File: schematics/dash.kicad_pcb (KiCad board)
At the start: 2 copper layers, 43.1 x 26.8 mm, 32 parts, among them J1 BATT_CONN, J2 EXTERNAL_TRIGGER, J3 USB_OTG, J4 Conn_01x08, J5 Conn_01x08, SW1 SW_Push, U1 ESP-12E, U2 ch340g, U3 MCP73833, U4 HT7333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

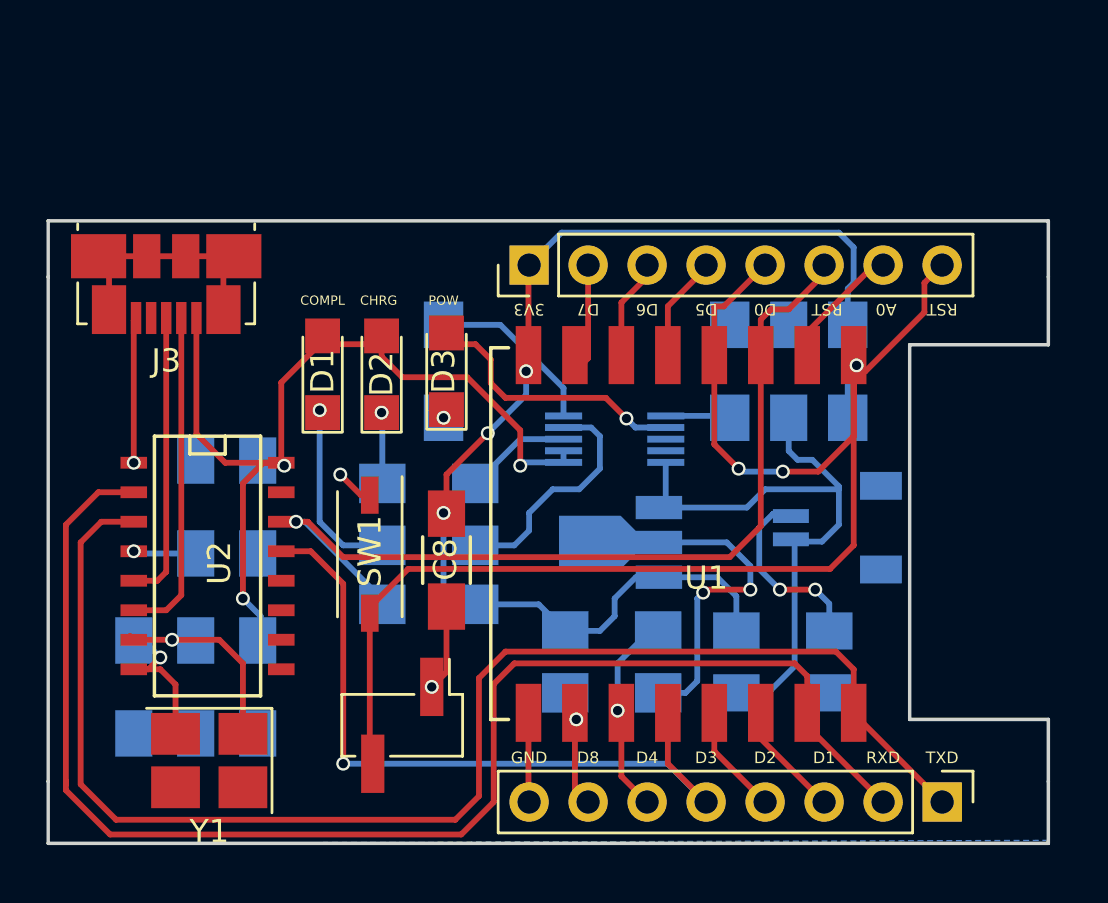
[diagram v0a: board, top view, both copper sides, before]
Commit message: [enh] Changed pcb size
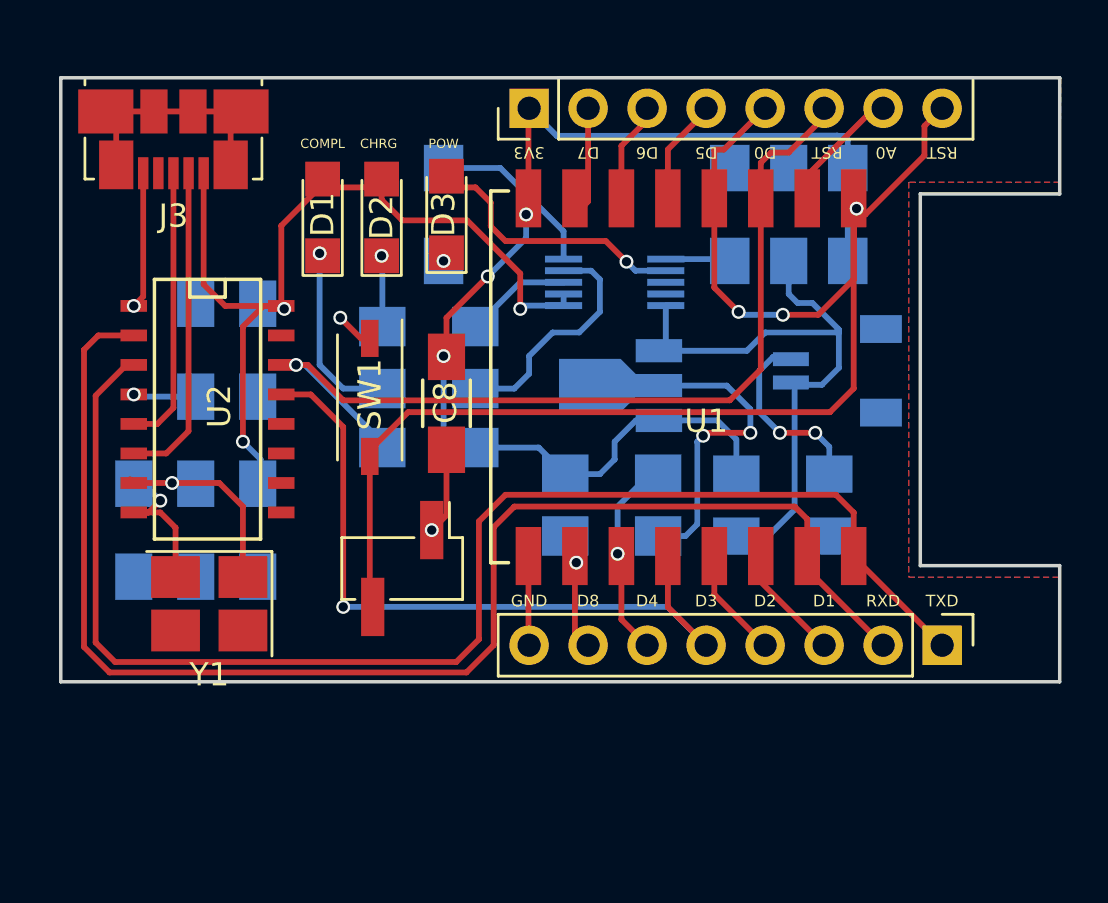
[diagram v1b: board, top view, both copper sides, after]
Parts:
- moved C1 6.75 mm to (163.7, 96.2)
- moved C2 6.75 mm to (138.2, 109.8)
- moved C3 6.75 mm to (135.5, 109.8)
- moved C4 6.75 mm to (140.8, 102.1)
- moved C5 6.75 mm to (140.8, 109.8)
- moved C6 6.75 mm to (138.2, 102.1)
- moved C7 6.75 mm to (163.4, 110.1)
- moved C8 6.75 mm to (149.0, 104.4)
- moved C9 6.75 mm to (163.4, 107.4)
- moved D1 6.75 mm to (143.6, 96.4)
- moved D2 6.75 mm to (146.2, 96.4)
- moved D3 6.75 mm to (149.0, 96.2)
- moved G*** 6.75 mm to (146.4, 110.7)
- moved J1 6.75 mm to (165.7, 103.0)
- moved J2 6.75 mm to (147.1, 111.5)
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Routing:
- net +3V3: track 52.4 -> 49.7 mm
- net /TXD: track 60.6 -> 59.4 mm
- net /RXD: track 61.6 -> 60.5 mm
- net +5V: track 40.0 -> 39.3 mm
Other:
- board size 43.1 x 26.8 mm -> 43 x 26 mm

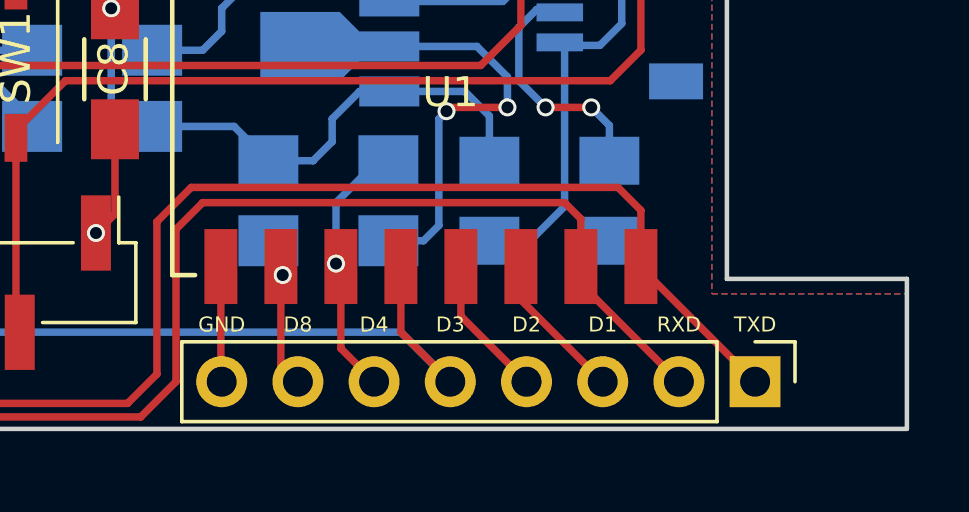
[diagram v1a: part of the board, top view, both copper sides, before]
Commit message: [add] Dimensions to pcb layout
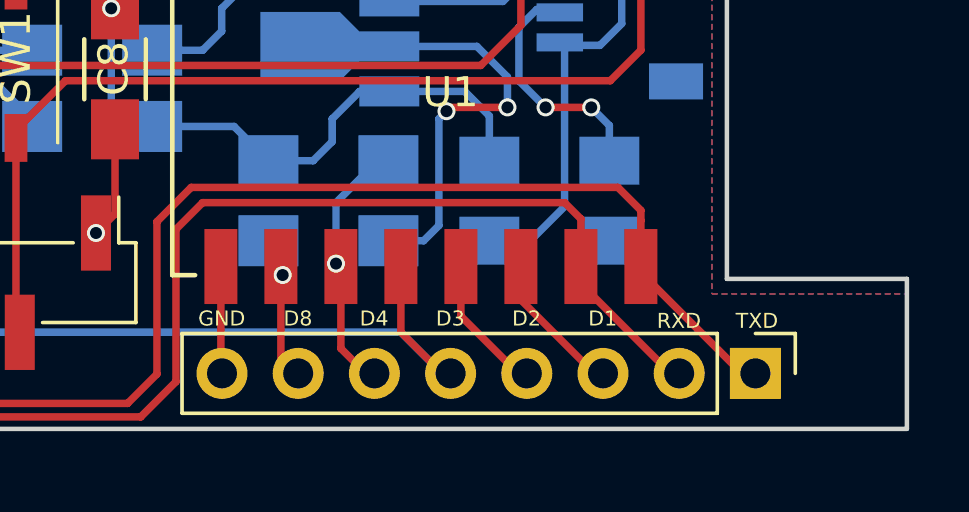
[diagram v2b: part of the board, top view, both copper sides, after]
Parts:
- moved J5 0.28 mm to (170.3, 114.5)
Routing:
- net /TXD: track 59.4 -> 60.1 mm
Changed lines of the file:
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@@
     (links 84)
     (no_connects 0)
-    (area 132.291999 90.286999 175.442001 116.437001)
+    (area 132.267715 86.133428 175.475001 119.259619)
     (thickness 1.6)
-    (drawings 28)
-    (tracks 311)
+    (drawings 32)
+    (tracks 314)
     (zones 0)
     (modules 32)
@@
     (pad_to_mask_clearance 0.2)
     (aux_axis_origin 132.367 116.362)
-    (grid_origin 142.367 102.362)
     (visible_elements FFFFFF7F)
     (pcbplotparams
@@
   )
   (module Pin_Headers:Pin_Header_Straight_1x08_Pitch2.54mm (layer F.Cu)
-    (at 170.307 114.789 270)
+    (at 170.317 114.512 270)
     (descr "Through hole straight pin header, 1x08, 2.54mm pitch, single row")
     (tags "Through hole pin header THT 1x08 2.54mm single row")
@@
     )
   )
+  (dimension 5 (width 0.3) (layer Cmts.User)
+    (gr_text "5.000 mm" (at 188.717 92.862 270) (layer Cmts.User)
+      (effects (font (size 1.5 1.5) (thickness 0.3)))
+    )
+    (feature1 (pts (xy 175.367 95.362) (xy 190.067 95.362)))
+    (feature2 (pts (xy 175.367 90.362) (xy 190.067 90.362)))
+    (crossbar (pts (xy 187.367 90.362) (xy 187.367 95.362)))
+    (arrow1a (pts (xy 187.367 95.362) (xy 186.780579 94.235496)))
+    (arrow1b (pts (xy 187.367 95.362) (xy 187.953421 94.235496)))
+    (arrow2a (pts (xy 187.367 90.362) (xy 186.780579 91.488504)))
+    (arrow2b (pts (xy 187.367 90.362) (xy 187.953421 91.488504)))
+  )
+  (dimension 16 (width 0.3) (layer Cmts.User)
+    (gr_text "16.000 mm" (at 182.717 103.362 270) (layer Cmts.User)
+      (effects (font (size 1.5 1.5) (thickness 0.3)))
+    )
+    (feature1 (pts (xy 175.367 111.362) (xy 184.067 111.362)))
+    (feature2 (pts (xy 175.367 95.362) (xy 184.067 95.362)))
+    (crossbar (pts (xy 181.367 95.362) (xy 181.367 111.362)))
+    (arrow1a (pts (xy 181.367 111.362) (xy 180.780579 110.235496)))
+    (arrow1b (pts (xy 181.367 111.362) (xy 181.953421 110.235496)))
+    (arrow2a (pts (xy 181.367 95.362) (xy 180.780579 96.488504)))
+    (arrow2b (pts (xy 181.367 95.362) (xy 181.953421 96.488504)))
+  )
+  (dimension 43 (width 0.3) (layer Cmts.User)
+    (gr_text "43.000 mm" (at 153.867 83.012) (layer Cmts.User)
+      (effects (font (size 1.5 1.5) (thickness 0.3)))
+    )
+    (feature1 (pts (xy 132.367 90.362) (xy 132.367 81.662)))
+    (feature2 (pts (xy 175.367 90.362) (xy 175.367 81.662)))
+    (crossbar (pts (xy 175.367 84.362) (xy 132.367 84.362)))
+    (arrow1a (pts (xy 132.367 84.362) (xy 133.493504 83.775579)))
+    (arrow1b (pts (xy 132.367 84.362) (xy 133.493504 84.948421)))
+    (arrow2a (pts (xy 175.367 84.362) (xy 174.240496 83.775579)))
+    (arrow2b (pts (xy 175.367 84.362) (xy 174.240496 84.948421)))
+  )
+  (dimension 26 (width 0.3) (layer Cmts.User)
+    (gr_text "26.000 mm" (at 125.017 103.362 90) (layer Cmts.User)
+      (effects (font (size 1.5 1.5) (thickness 0.3)))
+    )
+    (feature1 (pts (xy 132.367 90.362) (xy 123.667 90.362)))
+    (feature2 (pts (xy 132.367 116.362) (xy 123.667 116.362)))
+    (crossbar (pts (xy 126.367 116.362) (xy 126.367 90.362)))
+    (arrow1a (pts (xy 126.367 90.362) (xy 126.953421 91.488504)))
+    (arrow1b (pts (xy 126.367 90.362) (xy 125.780579 91.488504)))
+    (arrow2a (pts (xy 126.367 116.362) (xy 126.953421 115.235496)))
+    (arrow2b (pts (xy 126.367 116.362) (xy 125.780579 115.235496)))
+  )
   (gr_line (start 132.367 90.362) (end 132.367 116.362) (layer Edge.Cuts) (width 0.15))
   (gr_line (start 175.367 90.362) (end 132.367 90.362) (layer Edge.Cuts) (width 0.15))
@@
     (effects (font (size 0.5 0.5) (thickness 0.125)))
   )
-  (gr_text TXD (at 170.307 112.884) (layer F.SilkS)
+  (gr_text TXD (at 170.367 112.762) (layer F.SilkS)
     (effects (font (size 0.5 0.5) (thickness 0.125)))
   )
-  (gr_text RXD (at 167.767 112.884) (layer F.SilkS)
+  (gr_text RXD (at 167.767 112.762) (layer F.SilkS)
     (effects (font (size 0.5 0.5) (thickness 0.125)))
   )
-  (gr_text D1 (at 165.227 112.884) (layer F.SilkS)
+  (gr_text D1 (at 165.227 112.684) (layer F.SilkS)
     (effects (font (size 0.5 0.5) (thickness 0.125)))
   )
-  (gr_text D2 (at 162.687 112.884) (layer F.SilkS)
+  (gr_text D2 (at 162.687 112.684) (layer F.SilkS)
     (effects (font (size 0.5 0.5) (thickness 0.125)))
   )
-  (gr_text D3 (at 160.147 112.884) (layer F.SilkS)
+  (gr_text D3 (at 160.147 112.684) (layer F.SilkS)
     (effects (font (size 0.5 0.5) (thickness 0.125)))
   )
-  (gr_text D4 (at 157.607 112.884) (layer F.SilkS)
+  (gr_text D4 (at 157.607 112.684) (layer F.SilkS)
     (effects (font (size 0.5 0.5) (thickness 0.125)))
   )
-  (gr_text D8 (at 155.067 112.884) (layer F.SilkS)
+  (gr_text D8 (at 155.067 112.684) (layer F.SilkS)
     (effects (font (size 0.5 0.5) (thickness 0.125)))
   )
-  (gr_text GND (at 152.527 112.884) (layer F.SilkS)
+  (gr_text GND (at 152.527 112.684) (layer F.SilkS)
     (effects (font (size 0.5 0.5) (thickness 0.125)))
   )
@@
   (segment (start 164.5 111.522) (end 167.767 114.789) (width 0.25) (layer F.Cu) (net 19))
   (segment (start 135.509 101.454) (end 135.001 101.454) (width 0.25) (layer F.Cu) (net 19) (status 30))
+  (segment (start 166.5 110.25) (end 166.5 111.145) (width 0.25) (layer F.Cu) (net 20))
+  (segment (start 166.5 111.145) (end 169.867 114.512) (width 0.25) (layer F.Cu) (net 20))
+  (segment (start 169.867 114.512) (end 170.317 114.512) (width 0.25) (layer F.Cu) (net 20))
+  (segment (start 166.5 109.412) (end 166.5 109.077) (width 0.25) (layer F.Cu) (net 20))
+  (segment (start 166.5 109.412) (end 166.5 110.25) (width 0.25) (layer F.Cu) (net 20))
   (segment (start 135.1915 102.724) (end 135.509 102.724) (width 0.25) (layer F.Cu) (net 20))
   (segment (start 149.391011 115.511989) (end 134.707989 115.511989) (width 0.25) (layer F.Cu) (net 20))
@@
   (segment (start 133.867 104.0485) (end 135.1915 102.724) (width 0.25) (layer F.Cu) (net 20))
   (segment (start 166.5 109.077) (end 165.735 108.312) (width 0.25) (layer F.Cu) (net 20))
-  (segment (start 166.5 110.25) (end 166.5 109.077) (width 0.25) (layer F.Cu) (net 20))
   (segment (start 134.707989 115.511989) (end 133.867 114.671) (width 0.25) (layer F.Cu) (net 20))
   (segment (start 133.867 114.671) (end 133.867 104.0485) (width 0.25) (layer F.Cu) (net 20))
   (segment (start 166.5 110.25) (end 166.5 110.982) (width 0.25) (layer F.Cu) (net 20))
-  (segment (start 166.5 110.982) (end 170.307 114.789) (width 0.25) (layer F.Cu) (net 20))
   (segment (start 138.517 94.472) (end 138.517 99.255) (width 0.25) (layer F.Cu) (net 21))
   (segment (start 138.517 99.255) (end 139.446 100.184) (width 0.25) (layer F.Cu) (net 21))

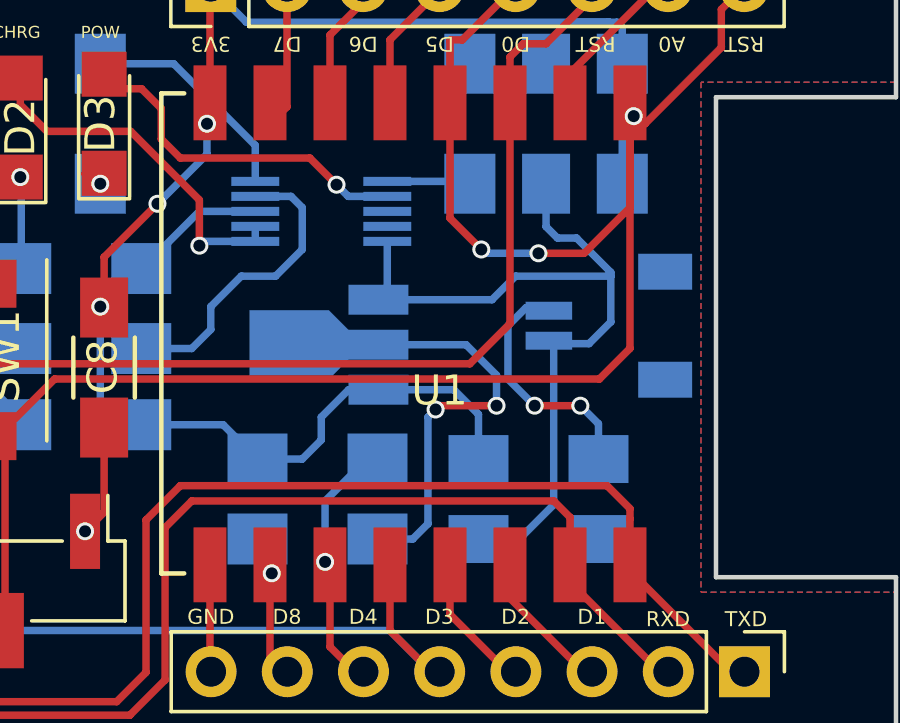
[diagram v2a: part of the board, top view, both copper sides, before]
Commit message: [fix] Better re-read those datasheets, wrong HT7333 pad mapping on the pcb
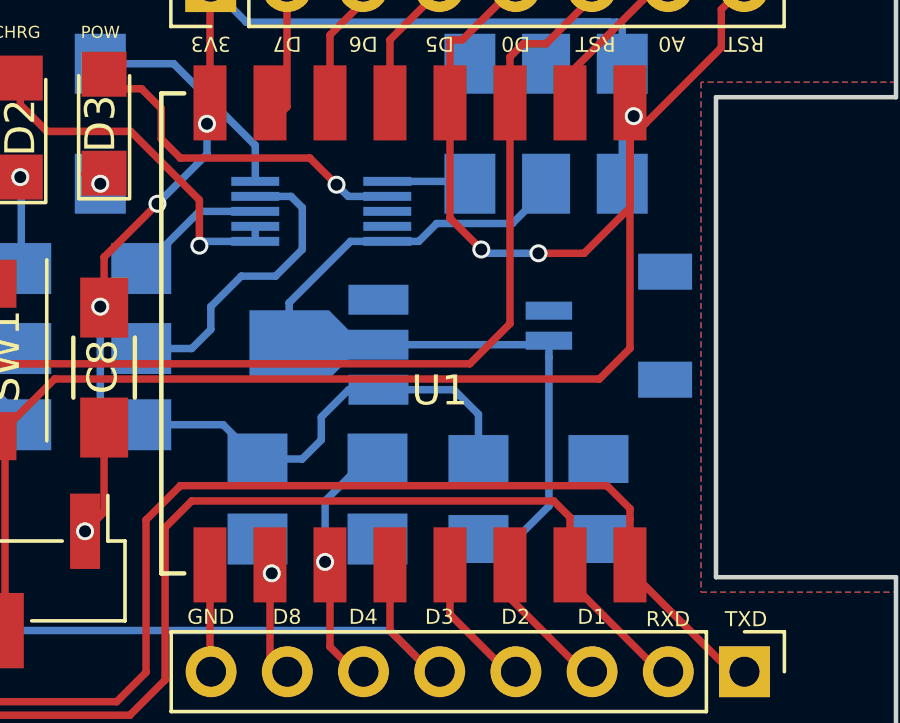
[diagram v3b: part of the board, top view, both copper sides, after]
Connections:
- U4 pad 1: Net-(C1-Pad1) -> GND
- U4 pad 2: GND -> Net-(C1-Pad1)
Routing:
- net GND: track 46.1 -> 24.6 mm, vias 7 -> 3
- net Net-(C1-Pad1): track 28.0 -> 28.8 mm

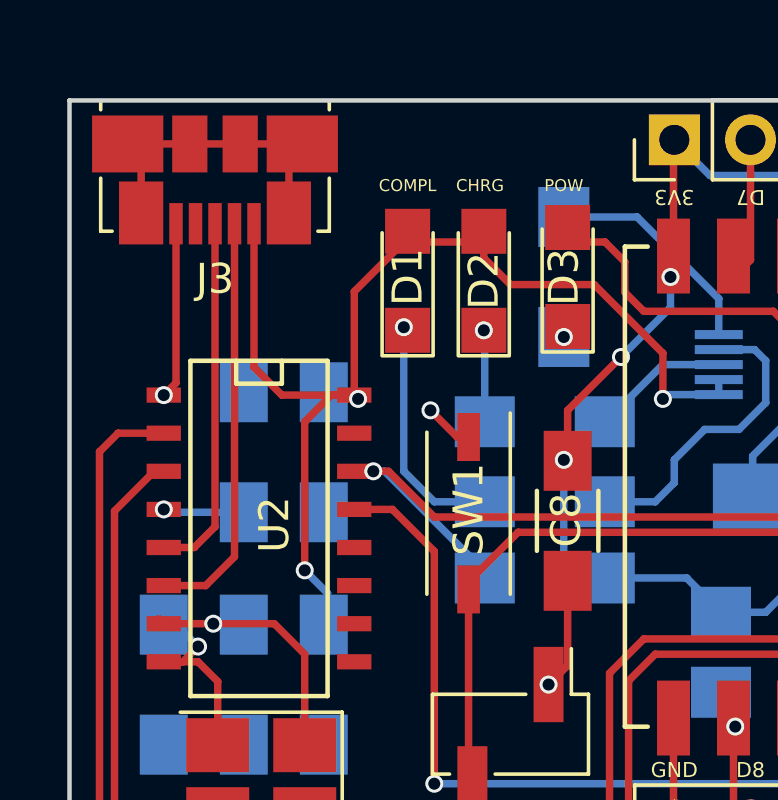
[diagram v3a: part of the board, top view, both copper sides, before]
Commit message: [fix] Change footprints to match component buyed
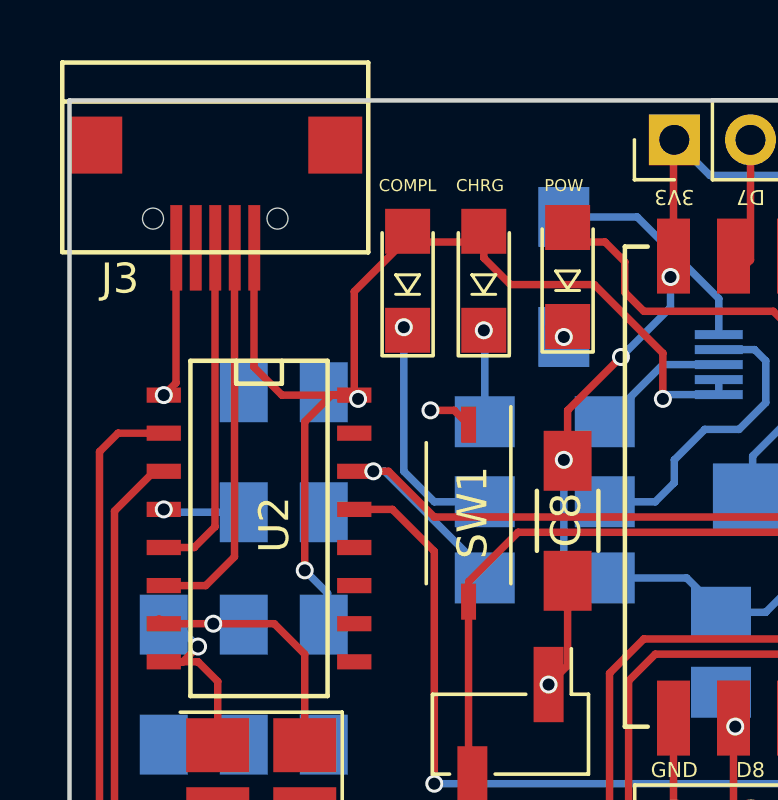
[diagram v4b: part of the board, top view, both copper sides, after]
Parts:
- J3: footprint Connectors_USB:USB_Micro-B_Molex_47346-0001 -> kicad-rleh/USB_Mikro_SMD_China.pretty:USB_Micro_SMD_China
- SW1: footprint Buttons_Switches_SMD:SW_DIP_x1_W5.08mm_Slide_Copal_CHS-A -> KiCad/Buttons_Switches_SMD.pretty:SW_DIP_x1_W5.9mm_Slide_Copal_CVS
- moved J3 2.71 mm to (137.2, 94.5), turned to 0 degrees
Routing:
- net Net-(J3-Pad6): track 10.8 -> 0.00 mm
